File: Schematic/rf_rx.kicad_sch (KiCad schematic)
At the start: 12 parts, among them SW2 TS24CA, U1 ME6217C33M5G, U12 ELRS_RX, U13 WIFI_RF_MODULE

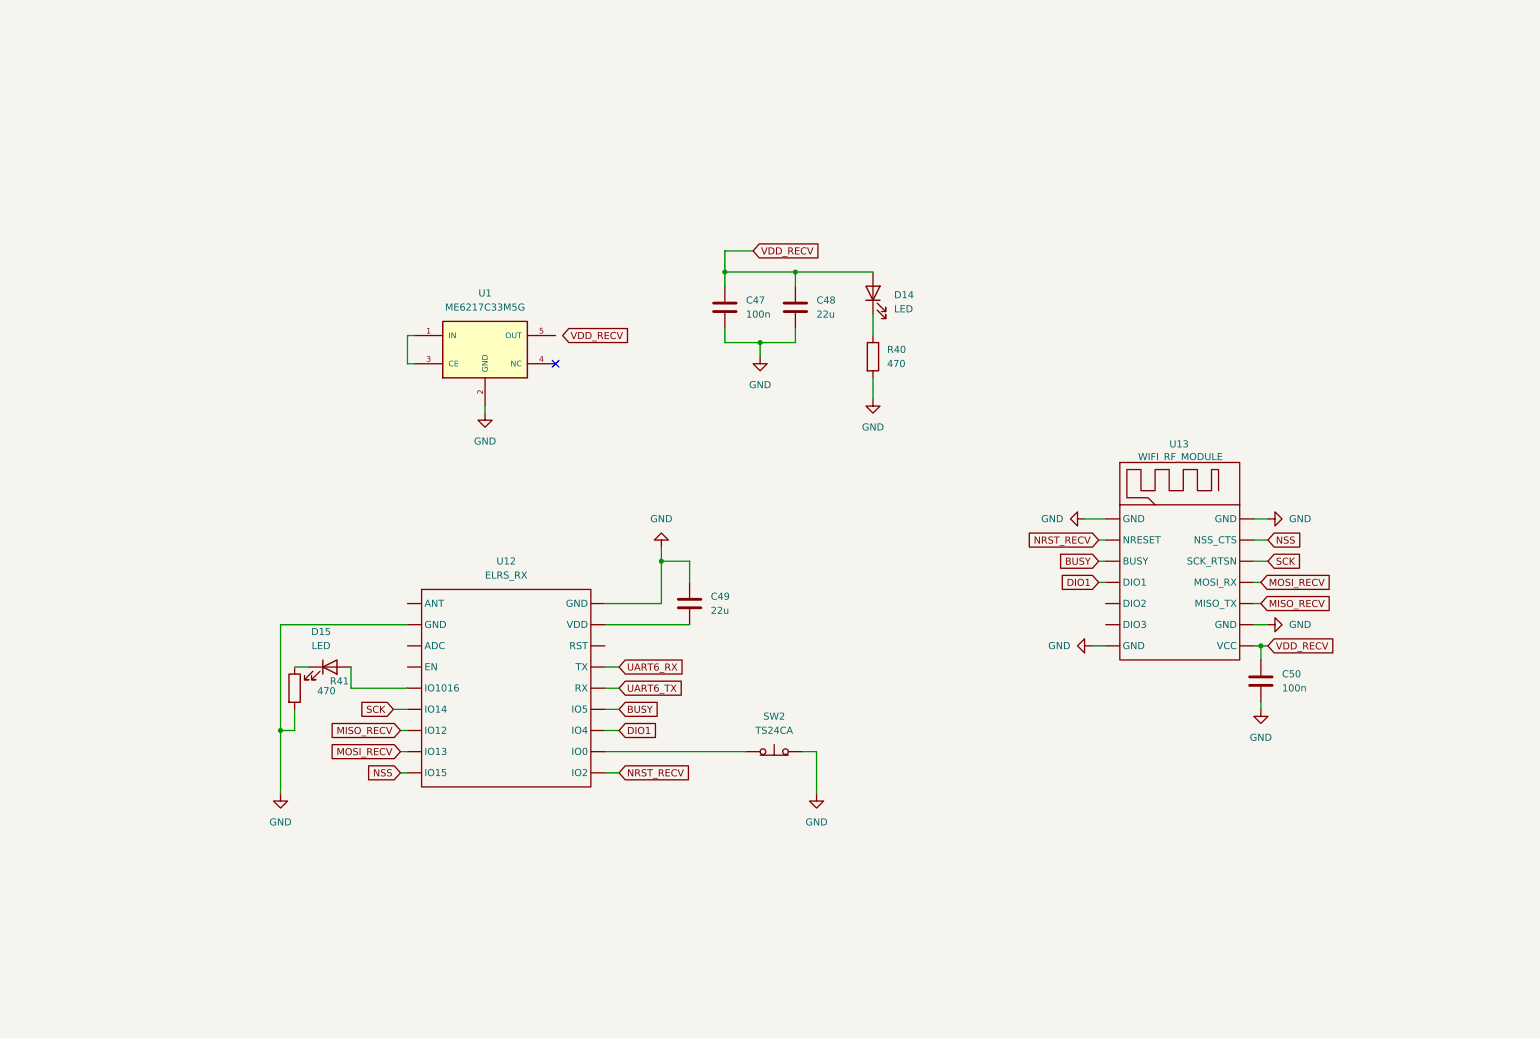
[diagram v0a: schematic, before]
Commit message: schematic fully finished, every footprint assigned, still electrical checking to do
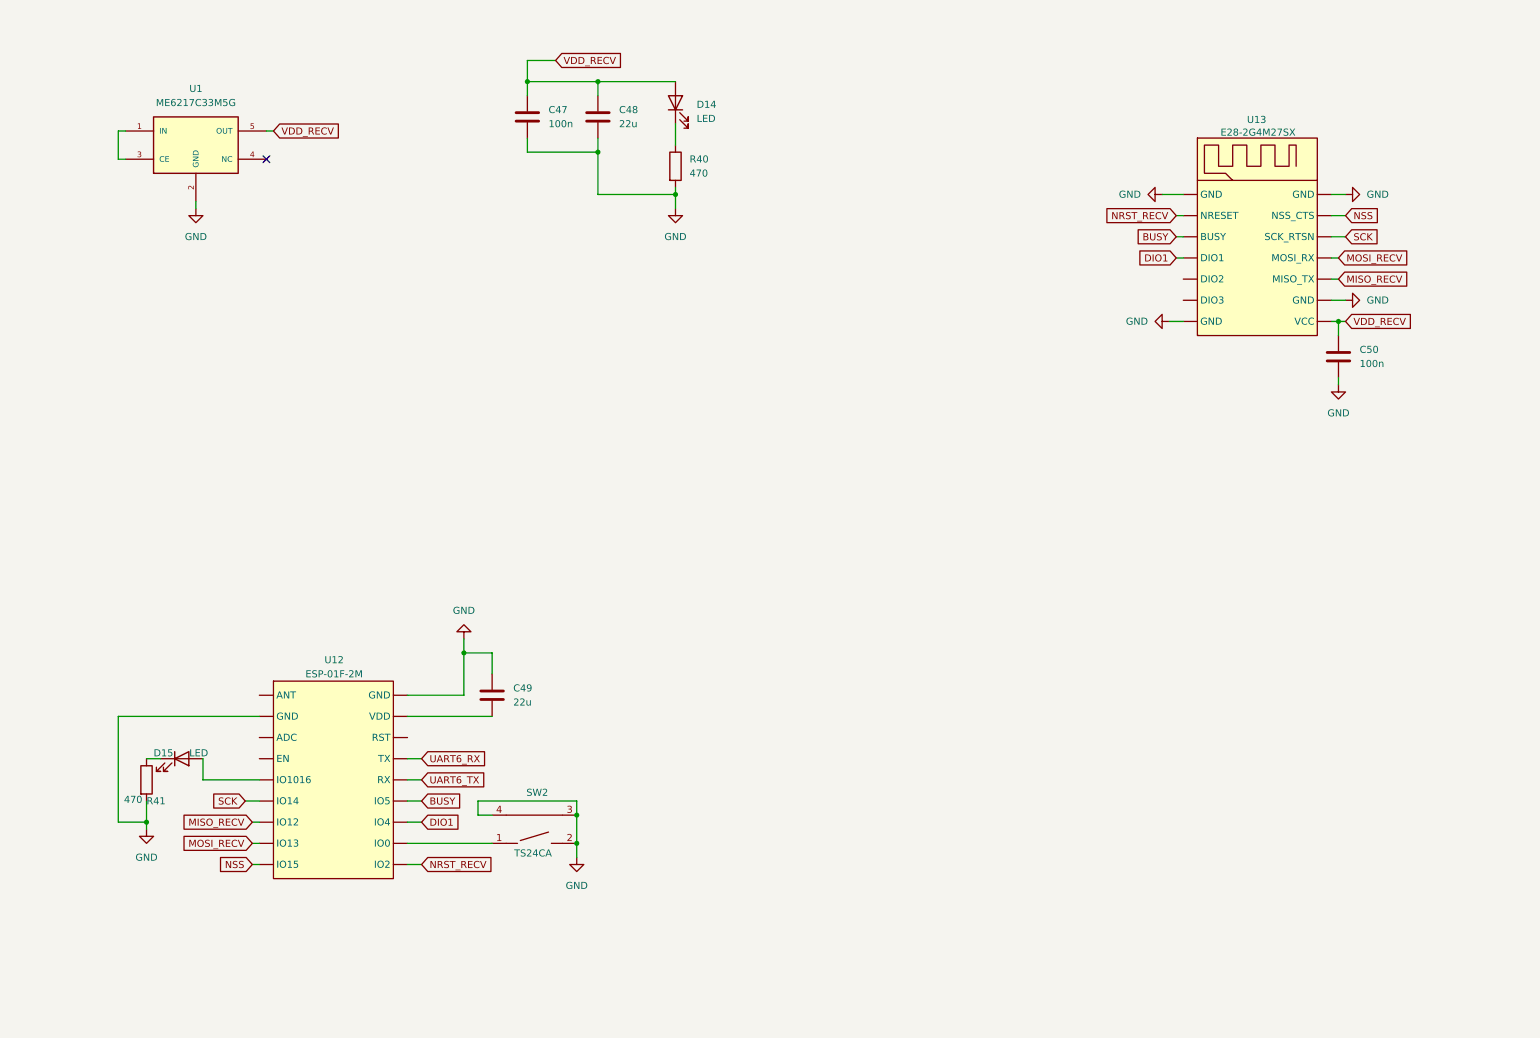
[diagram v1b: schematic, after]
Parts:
- removed SW2: TS24CA, symbol Switch:SW_Push_Open
- added SW2: TS24CA, ProLib_pcs_2025-11-24:SW-SMD_2P-TS24CA, symbol fch7_sym:TS24CA
- U12: value ELRS_RX -> ESP-01F-2M; footprint (none) -> fch7_fp:WIFIM-SMD_ESP-01F-2M
- U13: value WIFI_RF_MODULE -> E28-2G4M27SX; footprint (none) -> fch7_fp:WIRELM-SMD_E28-2G4M27SX
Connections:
- net GND: now also SW2.2, SW2.3, SW2.4
- net VDD_RECV: now also U1.5 (OUT)
- new net: SW2.1, U12. (IO2)
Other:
- moved on the sheet: C47, C48, C49, C50, D14, D15, R40, R41, U1

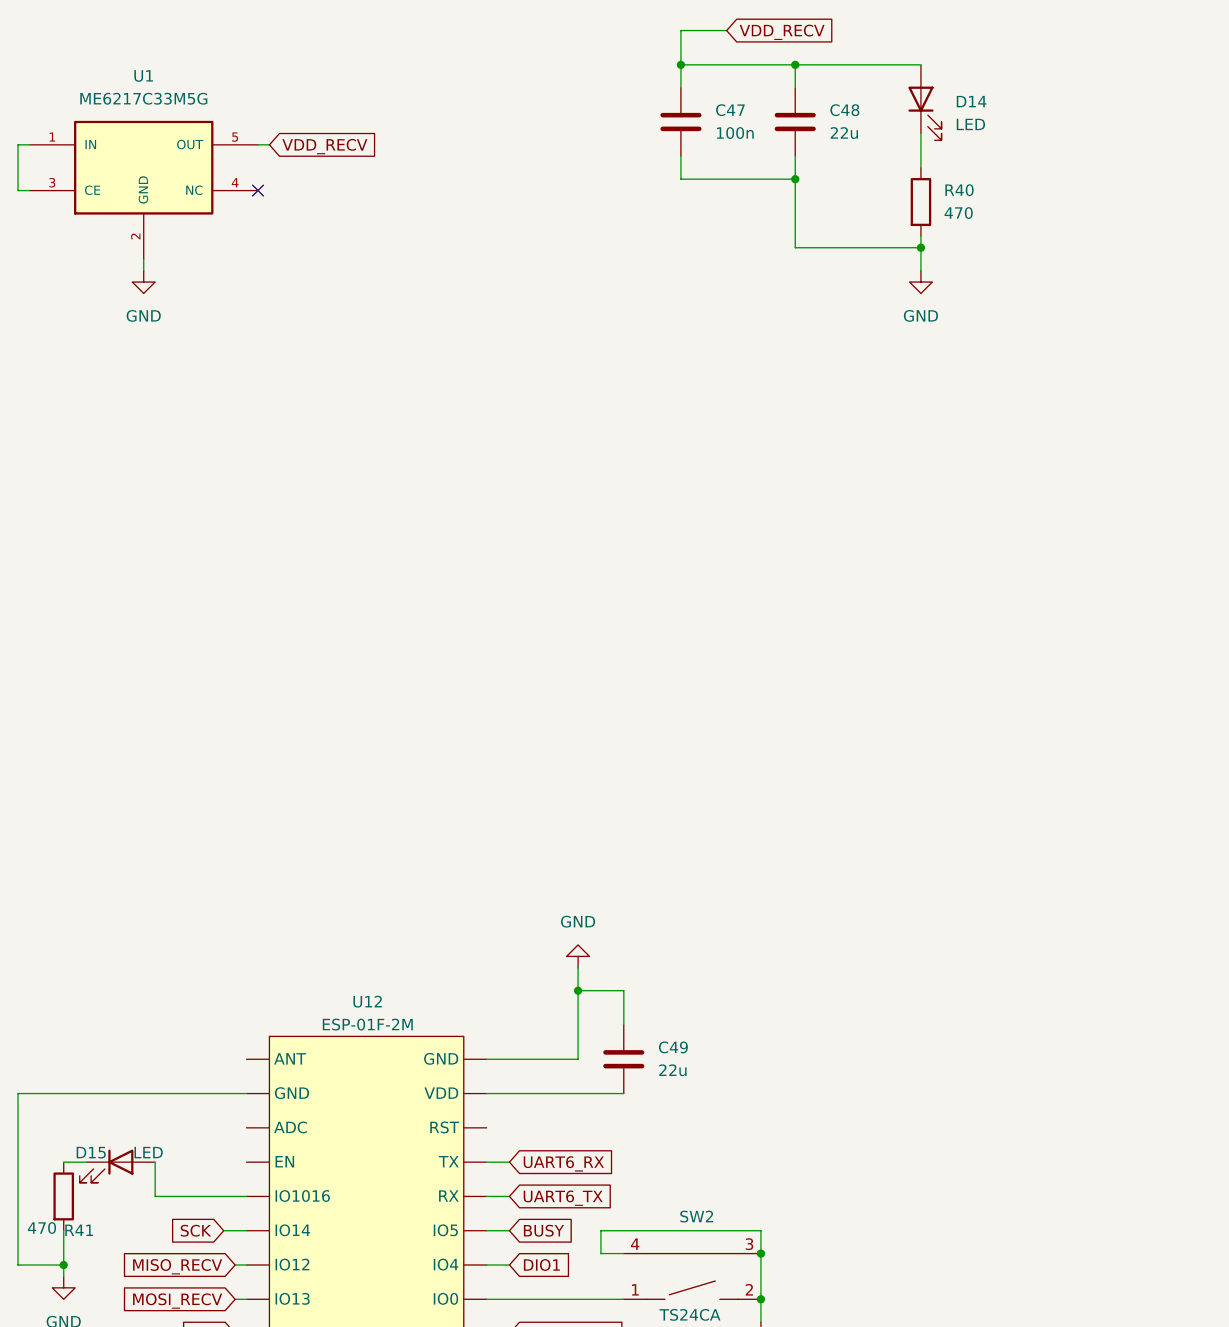
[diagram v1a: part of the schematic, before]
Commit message: reviewing and refactoring footprints and full schematic
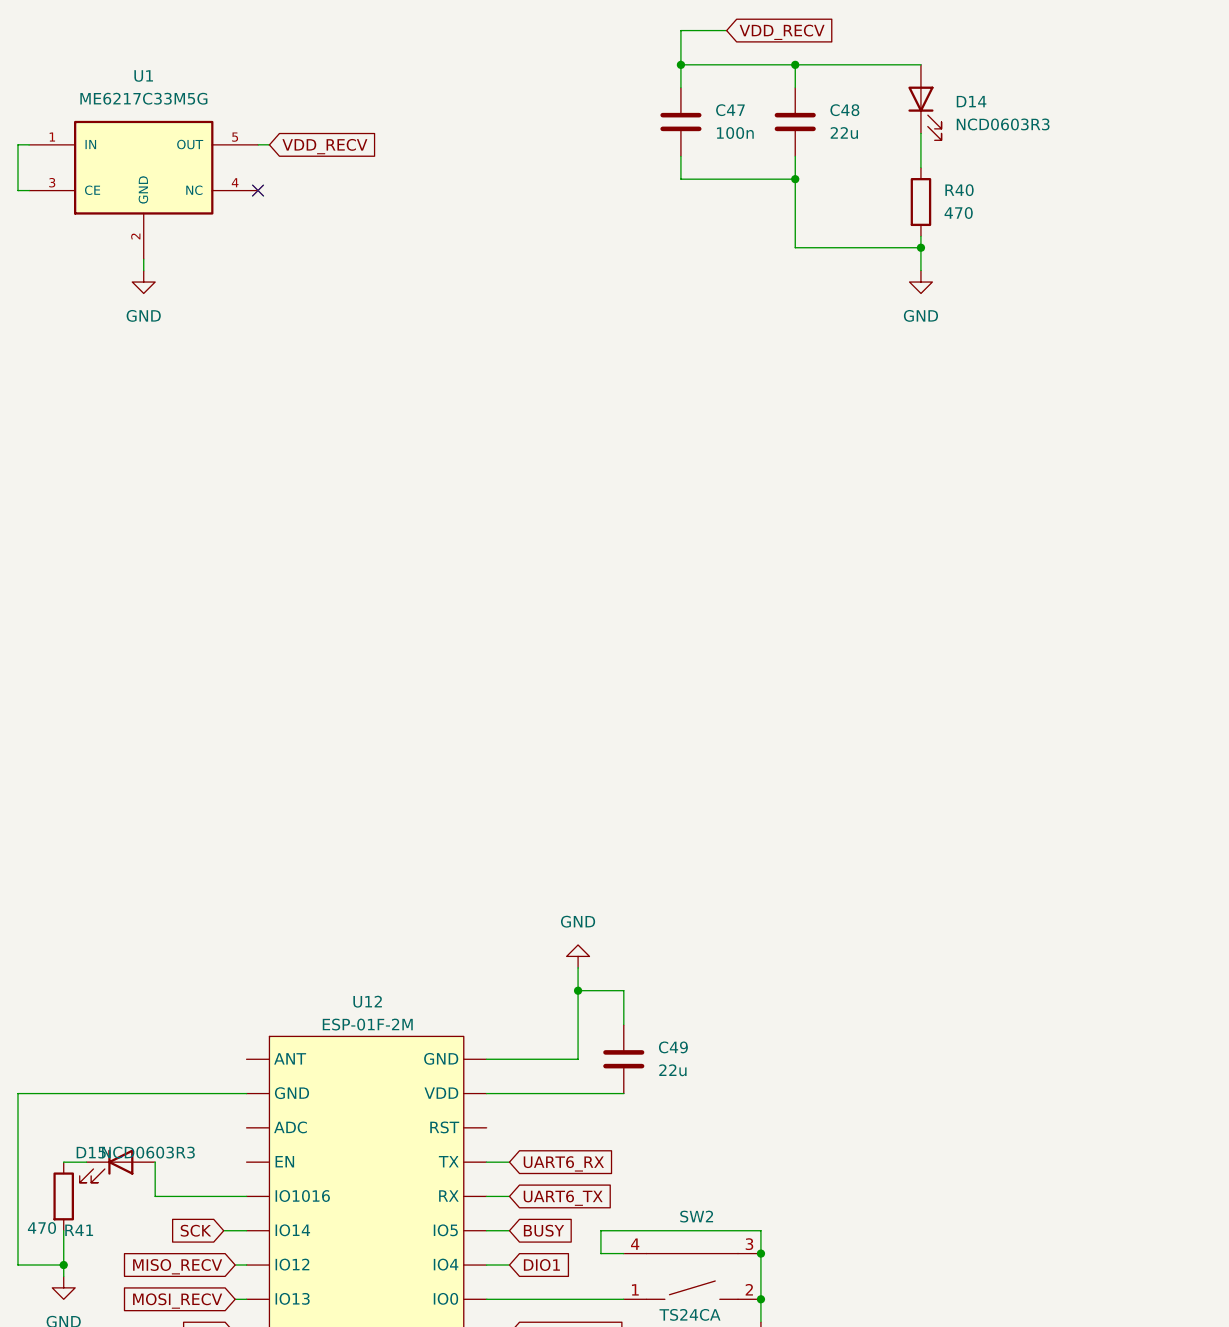
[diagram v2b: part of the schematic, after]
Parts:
- C47, C50: MPN (none) -> 0603B104K500NT; Manufacturer (none) -> FH
- C48, C49: footprint Capacitor_SMD:C_1210_3225Metric -> Capacitor_SMD:C_0805_2012Metric; MPN (none) -> CL21A226MAQNNNE; Manufacturer (none) -> SAMSUNG
- D14, D15: value LED -> NCD0603R3; footprint Diode_SMD:D_SOD-323 -> fch7_fp:LED0603-R-RD_RED; MPN (none) -> NCD0603R3; Manufacturer (none) -> NATIONSTAR
- R40, R41: MPN (none) -> 0603WAF4700T5E; Manufacturer (none) -> UNI-ROYAL
- SW2: MPN (none) -> TS24CA
- U1: MPN (none) -> ME6217C33M5G; Manufacturer (none) -> MICRONE; Price None -> (none)
- U12: MPN (none) -> ESP-01F-2M; Manufacturer (none) -> Ai-Thinker
- U13: MPN (none) -> E28-2G4M27SX; Manufacturer (none) -> EBYTE
